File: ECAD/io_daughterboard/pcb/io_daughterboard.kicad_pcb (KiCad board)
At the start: 2 copper layers, 120 x 66 mm, 90 parts, among them CON1 BARREL_JACK, P1 CONN_02X32, P10 Slave 5B, P11 Slave 1C, P12 Slave 3C, P13 Slave 4C, P14 Slave 5C, P15 Slave 1D, P16 Slave 3D, P17 Slave 4D, P18 Slave 5D, P2 CONN_02X32, P3 Slave 1A, P4 Slave 3A, P5 Slave 4A, P6 Slave 5A, P7 Slave 1B, P8 Slave 3B, P9 Slave 4B, U1 FAN5333BSX, U10 SN74LV1T34DCKR, U11 SN74LV1T34DCKR, U2 SPX3819M5-L-3-3, U3 74HC244, U4 74HC244, U5 74HC244, U6 STMPE811QTR, U7 74HC244, U8 74HC244, U9 74HC244

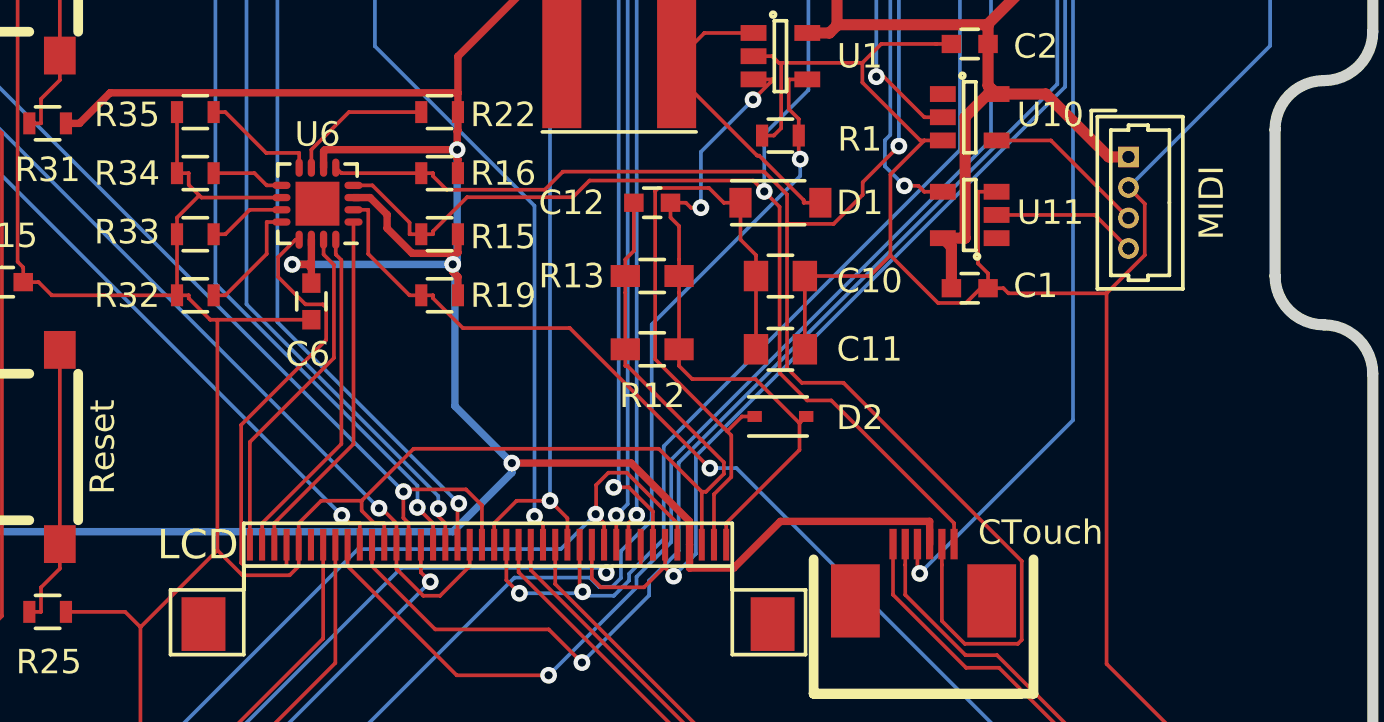
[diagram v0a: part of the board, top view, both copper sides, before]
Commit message: PCB and schematic had gotten out of sync.  Now in sync.
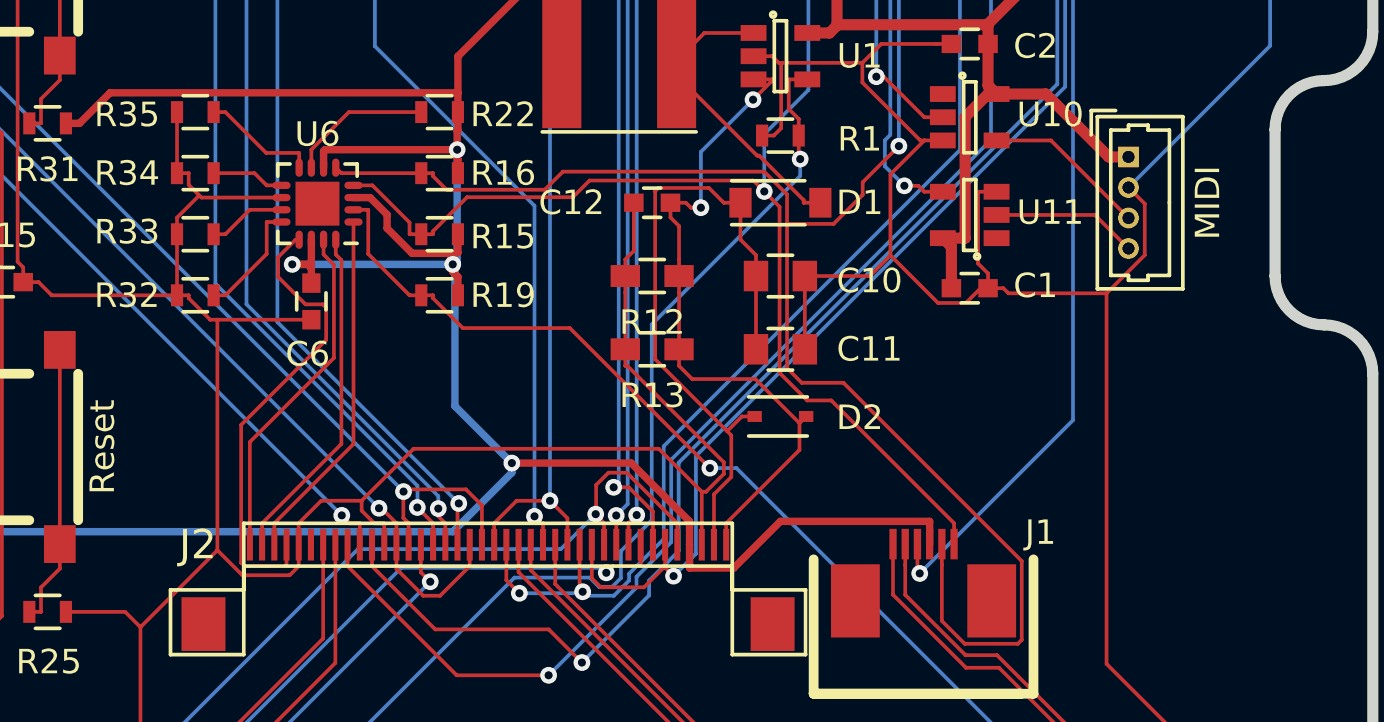
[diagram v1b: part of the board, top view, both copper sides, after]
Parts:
- P19: renamed from MIDI; value CONN_01X04 -> MIDI
- R12: footprint daughterfeet:R_0603_HandSoldering_no_paste -> Resistors_SMD:R_0603_HandSoldering
- R13: footprint Resistors_SMD:R_0603_HandSoldering -> daughterfeet:R_0603_HandSoldering_no_paste
- SW1: renamed from Reset; value Reset Button -> Reset
- SW2: renamed from User; value User Button -> User
- moved R12 3.00 mm to (190.5, 70.0)
- moved R13 3.00 mm to (190.5, 73.0)
- renumbered CTouch to J1, LCD to J2

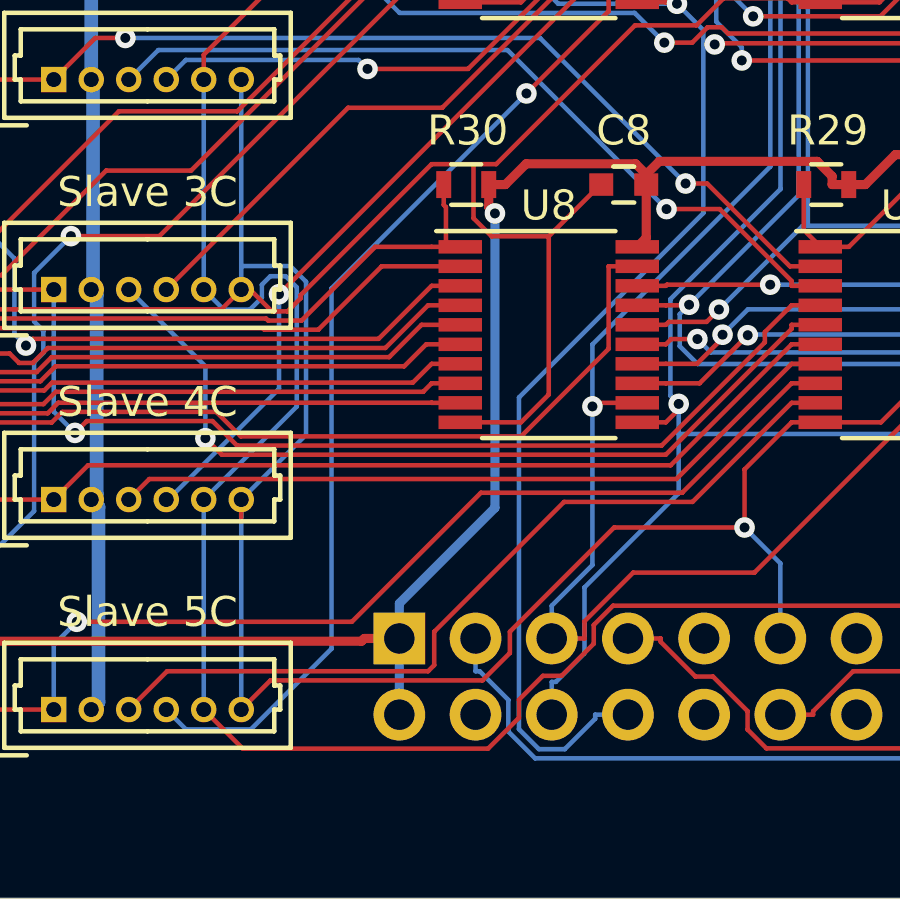
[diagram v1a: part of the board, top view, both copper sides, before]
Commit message: Disconnected +3.3V from P2.
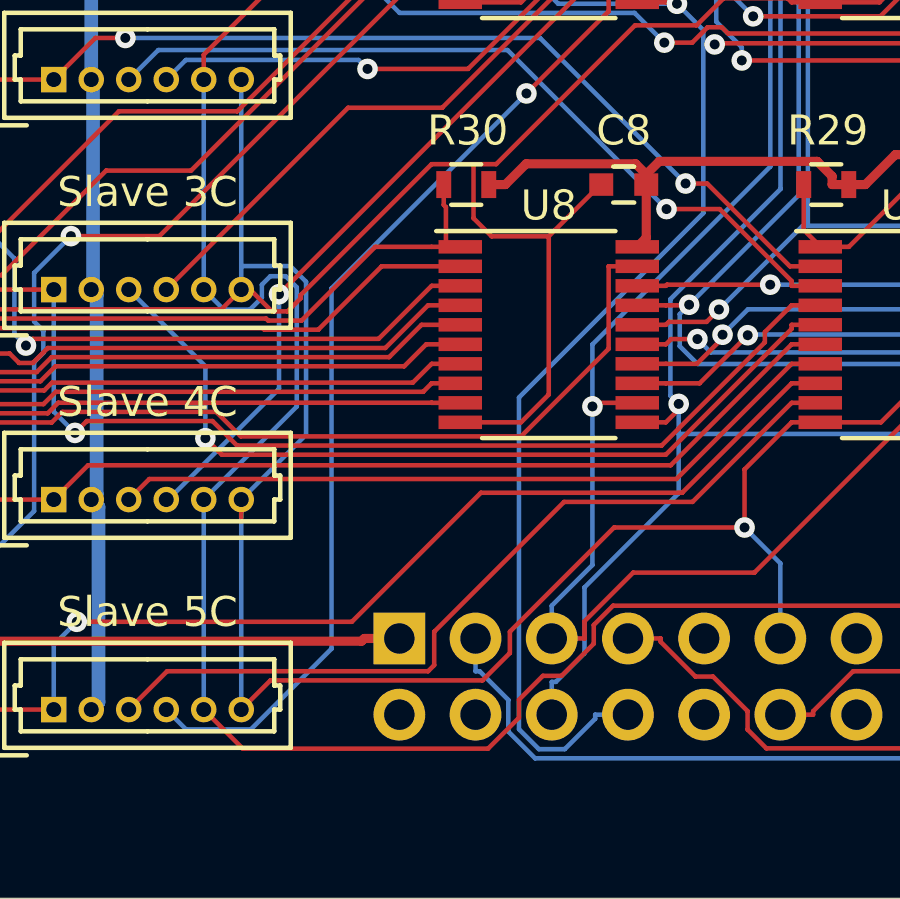
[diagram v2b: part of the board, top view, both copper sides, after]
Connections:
- P2 pad 1: +3V3 -> Net-(P2-Pad1)
- P2 pad 2: +3V3 -> Net-(P2-Pad2)
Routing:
- net +3V3: track 438.5 -> 404.7 mm, vias 6 -> 5
- net Net-(P2-Pad1): track 0.00 -> 14.7 mm
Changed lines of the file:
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@@
 (kicad_pcb (version 4) (host pcbnew 4.0.4-stable)
   (general
-    (links 360)
-    (no_connects 0)
+    (links 358)
+    (no_connects 1)
     (area 84.650001 26.3 231.421429 122.700001)
     (thickness 1.6)
     (drawings 24)
-    (tracks 2160)
+    (tracks 2152)
     (zones 0)
     (modules 90)
-    (nets 190)
+    (nets 192)
   )
   (page USLetter)
@@
   (net 188 "Net-(U11-Pad1)")
   (net 189 "Net-(J2-Pad35)")
+  (net 190 "Net-(P2-Pad1)")
+  (net 191 "Net-(P2-Pad2)")
   (net_class Default "This is the default net class."
     (clearance 0.1524)
@@
     (add_net "Net-(D1-Pad2)")
     (add_net "Net-(J2-Pad35)")
+    (add_net "Net-(P2-Pad1)")
+    (add_net "Net-(P2-Pad2)")
     (add_net "Net-(R22-Pad2)")
     (add_net "Net-(R25-Pad1)")
@@
     (fp_line (start -1.55 -1.55) (end -1.55 0) (layer B.SilkS) (width 0.15))
     (pad 1 thru_hole rect (at 0 0) (size 1.7272 1.7272) (drill 1.016) (layers *.Cu *.Mask)
-      (net 3 +3V3))
+      (net 190 "Net-(P2-Pad1)"))
     (pad 2 thru_hole oval (at 0 2.54) (size 1.7272 1.7272) (drill 1.016) (layers *.Cu *.Mask)
-      (net 3 +3V3))
+      (net 191 "Net-(P2-Pad2)"))
     (pad 3 thru_hole oval (at 2.54 0) (size 1.7272 1.7272) (drill 1.016) (layers *.Cu *.Mask)
       (net 83 /LCD_PWM))
@@
   (via (at 182.3348 69.5246) (size 0.6858) (layers F.Cu B.Cu) (net 3))
   (via (at 182.5158 64.829) (size 0.6858) (layers F.Cu B.Cu) (net 3))
-  (via (at 137.7064 76.9614) (size 0.6858) (layers F.Cu B.Cu) (net 3))
   (via (at 158.7742 80.2691) (size 0.6858) (layers F.Cu B.Cu) (net 3))
   (via (at 175.7638 69.5247) (size 0.6858) (layers F.Cu B.Cu) (net 3))
@@
   (segment (start 142.75 63.775) (end 142.45 64.075) (width 0.3048) (layer F.Cu) (net 3))
   (segment (start 142.75 62) (end 142.75 63.775) (width 0.3048) (layer F.Cu) (net 3))
-  (segment (start 134.52 91.13) (end 133.3513 91.13) (width 0.3048) (layer F.Cu) (net 3))
   (segment (start 104.7224 78.5551) (end 105 78.5551) (width 0.3048) (layer F.Cu) (net 3))
   (segment (start 104.2448 79.0327) (end 104.7224 78.5551) (width 0.3048) (layer F.Cu) (net 3))
@@
   (segment (start 105 84.4449) (end 104.2448 83.6897) (width 0.3048) (layer F.Cu) (net 3))
   (segment (start 105 85) (end 105 84.4449) (width 0.3048) (layer F.Cu) (net 3))
-  (segment (start 119.8149 91.13) (end 119.5 91.4449) (width 0.3048) (layer F.Cu) (net 3))
   (segment (start 119.5 85) (end 119.5 85.5551) (width 0.3048) (layer F.Cu) (net 3))
   (segment (start 192.03 81) (end 192.03 81.9551) (width 0.3048) (layer F.Cu) (net 3))
@@
   (segment (start 105 85.5551) (end 104.7224 85.5551) (width 0.3048) (layer F.Cu) (net 3))
   (segment (start 105 78) (end 105 78.5551) (width 0.3048) (layer F.Cu) (net 3))
-  (segment (start 118.6999 90.015) (end 119.8149 91.13) (width 0.3048) (layer F.Cu) (net 3))
-  (segment (start 118.6999 86.0777) (end 118.6999 90.015) (width 0.3048) (layer F.Cu) (net 3))
-  (segment (start 119.2225 85.5551) (end 118.6999 86.0777) (width 0.3048) (layer F.Cu) (net 3))
   (segment (start 119.5 85.5551) (end 119.2225 85.5551) (width 0.3048) (layer F.Cu) (net 3))
   (segment (start 119.5 92) (end 119.5 91.7224) (width 0.3048) (layer F.Cu) (net 3))
-  (segment (start 119.5 91.7224) (end 119.5 91.4449) (width 0.3048) (layer F.Cu) (net 3))
   (segment (start 104.7224 92.5551) (end 105 92.5551) (width 0.3048) (layer F.Cu) (net 3))
   (segment (start 104.2448 93.0327) (end 104.7224 92.5551) (width 0.3048) (layer F.Cu) (net 3))
@@
   (segment (start 154.75 76.8875) (end 154.75 77.775) (width 0.3048) (layer F.Cu) (net 3))
   (segment (start 161.5 83.75) (end 161.5 82.9949) (width 0.3048) (layer F.Cu) (net 3))
-  (segment (start 133.2595 91.2218) (end 133.3513 91.13) (width 0.3048) (layer F.Cu) (net 3))
-  (segment (start 119.9067 91.2218) (end 133.2595 91.2218) (width 0.3048) (layer F.Cu) (net 3))
-  (segment (start 119.8149 91.13) (end 119.9067 91.2218) (width 0.3048) (layer F.Cu) (net 3))
   (segment (start 182.547 68.2892) (end 182.547 69.0443) (width 0.3048) (layer F.Cu) (net 3))
   (segment (start 104.2448 76.6897) (end 105 77.4449) (width 0.3048) (layer F.Cu) (net 3))
@@
   (segment (start 105 46.5) (end 105.7551 46.5) (width 0.3048) (layer F.Cu) (net 3))
   (segment (start 137.5 76) (end 138.0551 76) (width 0.3048) (layer F.Cu) (net 3))
-  (segment (start 134.52 93.67) (end 134.52 91.13) (width 0.3048) (layer B.Cu) (net 3))
-  (segment (start 137.5 76) (end 137.5 76.7551) (width 0.3048) (layer F.Cu) (net 3))
-  (segment (start 134.52 91.13) (end 134.52 89.9613) (width 0.3048) (layer B.Cu) (net 3))
-  (segment (start 137.7064 86.7749) (end 137.7064 76.9614) (width 0.3048) (layer B.Cu) (net 3))
-  (segment (start 134.52 89.9613) (end 137.7064 86.7749) (width 0.3048) (layer B.Cu) (net 3))
-  (segment (start 137.7063 76.9614) (end 137.7064 76.9614) (width 0.3048) (layer F.Cu) (net 3))
-  (segment (start 137.5 76.7551) (end 137.7063 76.9614) (width 0.3048) (layer F.Cu) (net 3))
   (segment (start 154.75 63.775) (end 154.45 64.075) (width 0.3048) (layer F.Cu) (net 3))
   (segment (start 154.75 62) (end 154.75 63.775) (width 0.3048) (layer F.Cu) (net 3))
@@
   (segment (start 142.75 48.7981) (end 148.3499 48.7981) (width 0.3048) (layer F.Cu) (net 3))
   (segment (start 149.5 48) (end 148.9449 48) (width 0.3048) (layer F.Cu) (net 3))
+  (segment (start 119.2225 85.5551) (end 118.6999 86.0777) (width 0.3048) (layer F.Cu) (net 3))
+  (segment (start 119.5 91.7224) (end 119.5 91.4449) (width 0.3048) (layer F.Cu) (net 3))
+  (segment (start 119.8149 91.13) (end 119.5 91.4449) (width 0.3048) (layer F.Cu) (net 3))
+  (segment (start 118.6999 90.015) (end 119.8149 91.13) (width 0.3048) (layer F.Cu) (net 3))
+  (segment (start 118.6999 86.0777) (end 118.6999 90.015) (width 0.3048) (layer F.Cu) (net 3))
+  (segment (start 119.8149 91.13) (end 119.9067 91.2218) (width 0.3048) (layer F.Cu) (net 3))
   (segment (start 194.115 68.5111) (end 194.75 69.1461) (width 0.1524) (layer F.Cu) (net 4))
   (segment (start 194.115 67) (end 194.115 68.5111) (width 0.1524) (layer F.Cu) (net 4))
@@
   (segment (start 176.047 65.5642) (end 176.047 64.9603) (width 0.1524) (layer F.Cu) (net 186))
   (segment (start 172.547 63.2892) (end 173.0259 63.2892) (width 0.1524) (layer F.Cu) (net 186))
+  (segment (start 134.52 91.13) (end 133.3513 91.13) (width 0.3048) (layer F.Cu) (net 190))
+  (segment (start 133.2595 91.2218) (end 133.3513 91.13) (width 0.3048) (layer F.Cu) (net 190))
+  (segment (start 119.9067 91.2218) (end 133.2595 91.2218) (width 0.3048) (layer F.Cu) (net 190))
   (zone (net 2) (net_name GND) (layer F.Cu) (hatch edge 0.508)
     (connect_pads (clearance 0.1524))

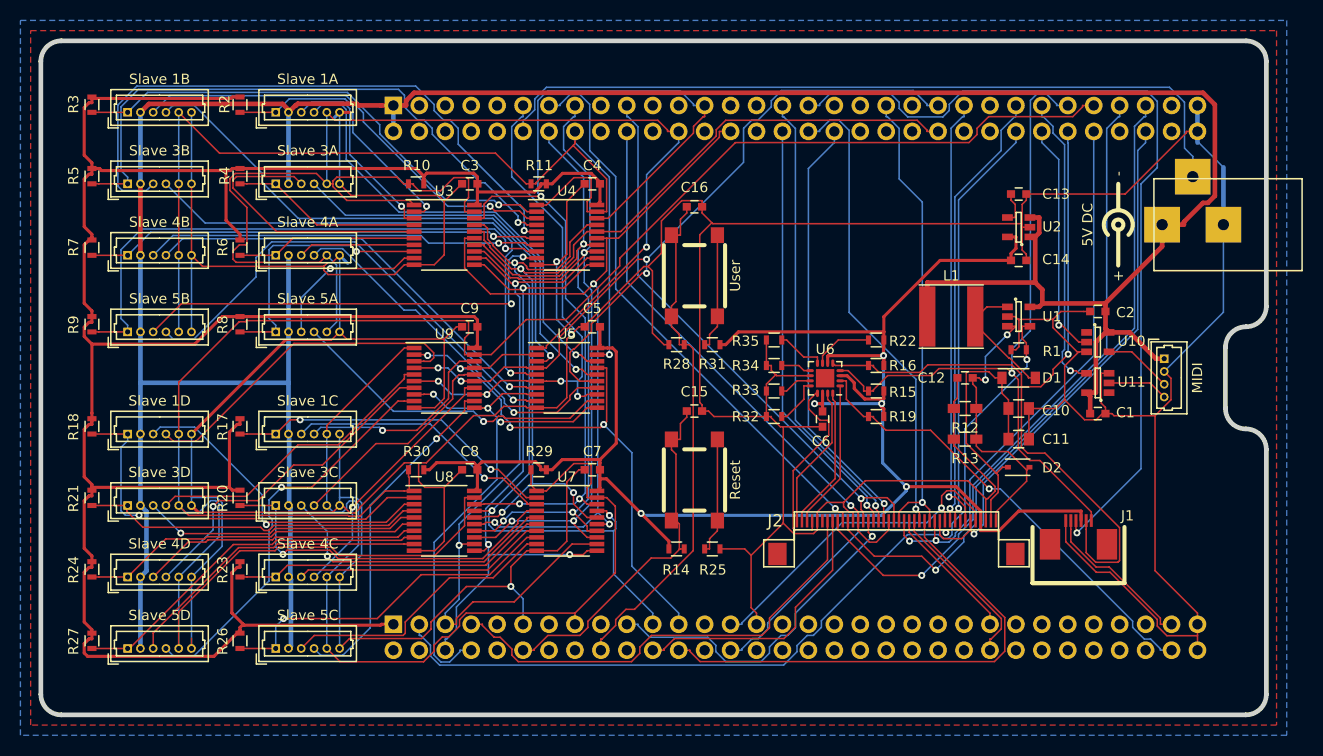
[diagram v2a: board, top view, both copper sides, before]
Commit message: Removed all traces and copper pours; reconnected filter caps.
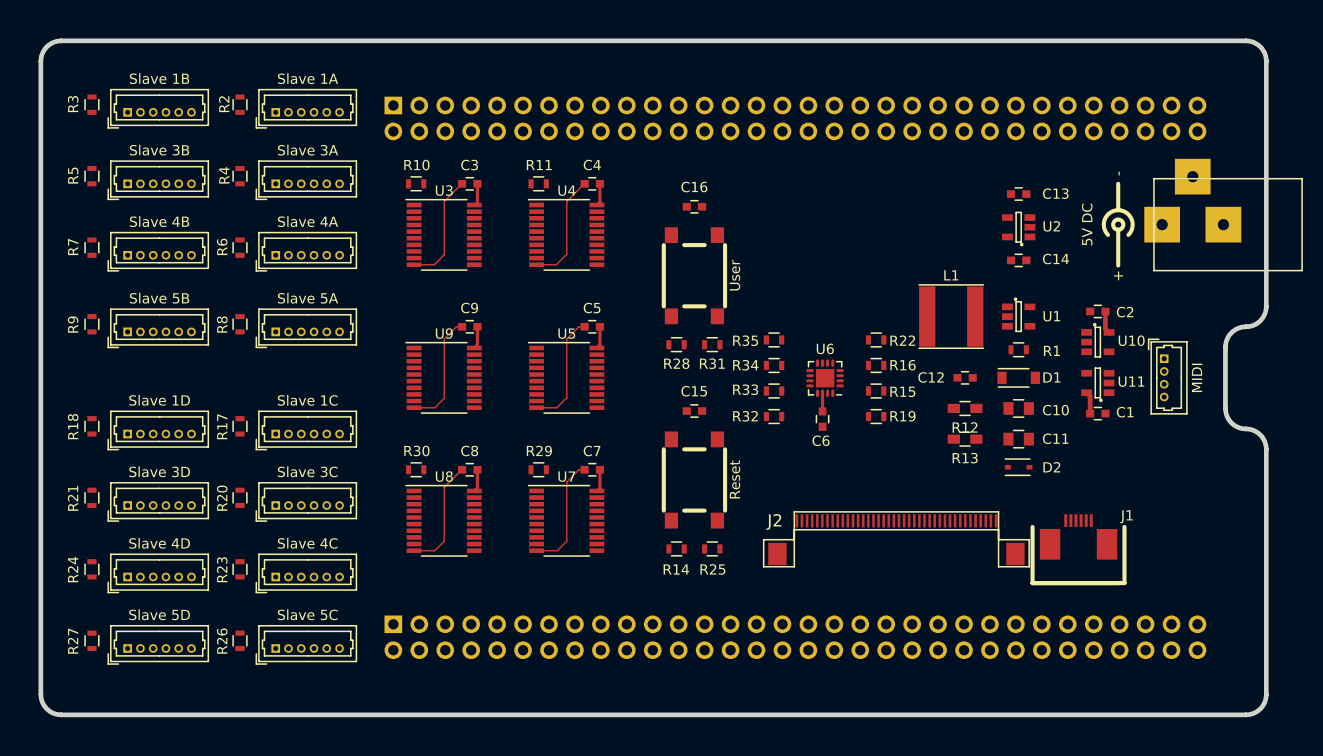
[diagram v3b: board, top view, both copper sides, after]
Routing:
- net GND: track 625.1 -> 67.2 mm, vias 3 -> 0
- net +3V3: track 404.7 -> 15.0 mm, vias 5 -> 0
- net +5V: track 299.9 -> 4.39 mm
- net /PC8: track 205.6 -> 0.00 mm
- net /PB7: track 136.2 -> 0.00 mm, vias 1 -> 0
- net /PE3: track 110.2 -> 0.00 mm, vias 1 -> 0
- net /PB4: track 95.3 -> 0.00 mm, vias 3 -> 0
- net /PC3: track 95.1 -> 0.00 mm
- net /PC11: track 92.3 -> 0.00 mm, vias 3 -> 0
- net /LCD_PWM: track 85.8 -> 0.00 mm, vias 1 -> 0
- net /PC12: track 85.1 -> 0.00 mm, vias 4 -> 0
- net /CTOUCH_WAKE: track 84.6 -> 0.00 mm, vias 1 -> 0
- net /PB3: track 79.1 -> 0.00 mm, vias 3 -> 0
- net /I²C3_SDA: track 77.7 -> 0.00 mm, vias 1 -> 0
- net /PC13: track 76.0 -> 0.00 mm
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- removed copper zone on B.Cu, net GND
- removed copper zone on F.Cu, net GND

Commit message: Autorouted.
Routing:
- net GND: track 67.2 -> 632.6 mm, vias 0 -> 1
- net +3V3: track 15.0 -> 394.0 mm, vias 0 -> 4
- net +5V: track 4.39 -> 286.9 mm
- net /PC8: track 0.00 -> 163.3 mm, vias 0 -> 3
- net /I²C3_SDA: track 0.00 -> 105.2 mm, vias 0 -> 1
- net /PE3: track 0.00 -> 104.4 mm, vias 0 -> 3
- net /PC12: track 0.00 -> 104.2 mm, vias 0 -> 3
- net /PB7: track 0.00 -> 101.0 mm, vias 0 -> 1
- net /PC11: track 0.00 -> 97.6 mm, vias 0 -> 3
- net /CTOUCH_WAKE: track 0.00 -> 94.9 mm
- net /PA7: track 0.00 -> 92.4 mm, vias 0 -> 3
- net /PA5: track 0.00 -> 89.5 mm, vias 0 -> 4
- net /PF7: track 0.00 -> 87.7 mm, vias 0 -> 2
- net /LCD_PWM: track 0.00 -> 85.5 mm, vias 0 -> 1
- net /PC3: track 0.00 -> 82.6 mm, vias 0 -> 3
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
